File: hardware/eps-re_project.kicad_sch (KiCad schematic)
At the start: 50 parts, among them J1 2053380004, J13 53398-0671, J14 53398-0471, J2 2053380004, J21 205338-0002, J22 205338-0002, J25 205338-0002, J26 205338-0002, J27 205338-0002, J28 205338-0002, J29 205338-0002, J3 53398-0471, J4 2053380004, J5 53398-0471, J6 53398-0471, J7 53398-0471

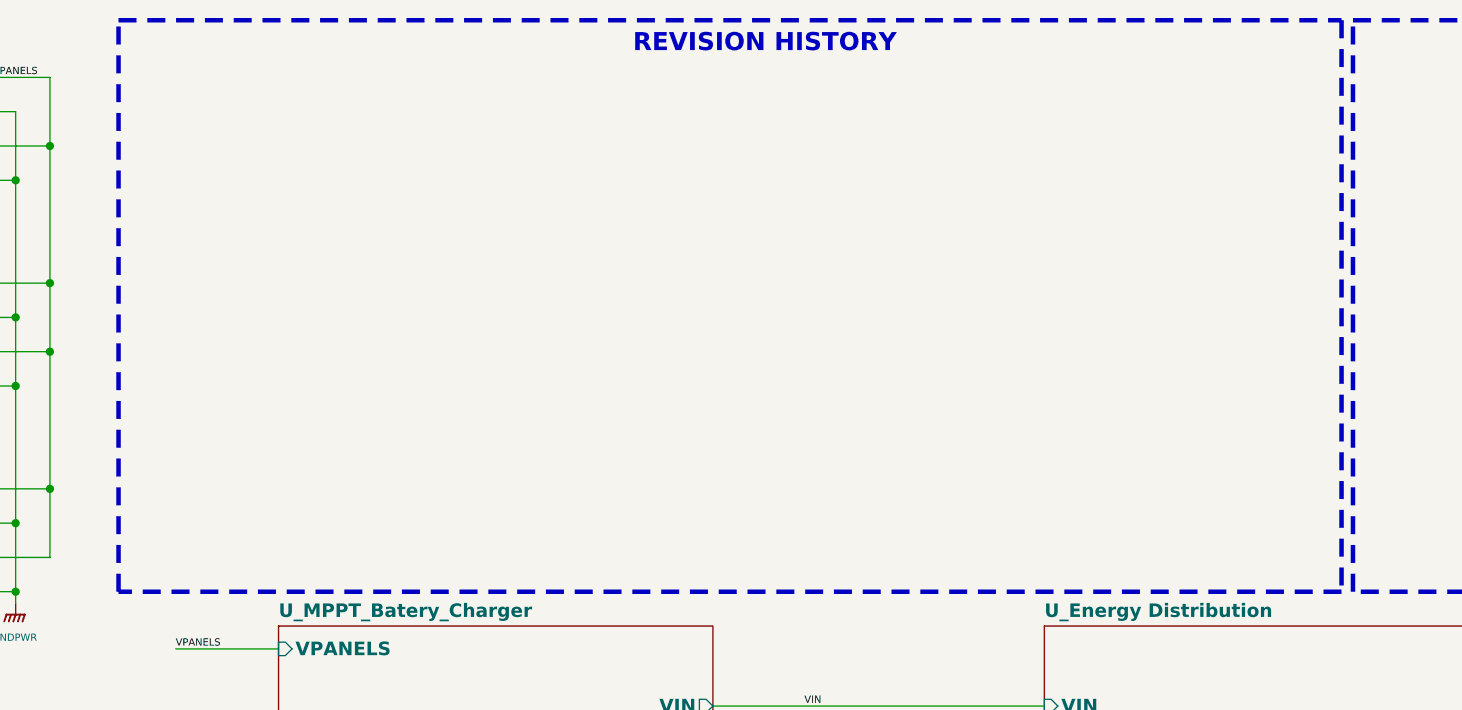
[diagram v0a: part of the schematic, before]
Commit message: hardware: Increasing the readability of the schematic and adding a table with the revision history
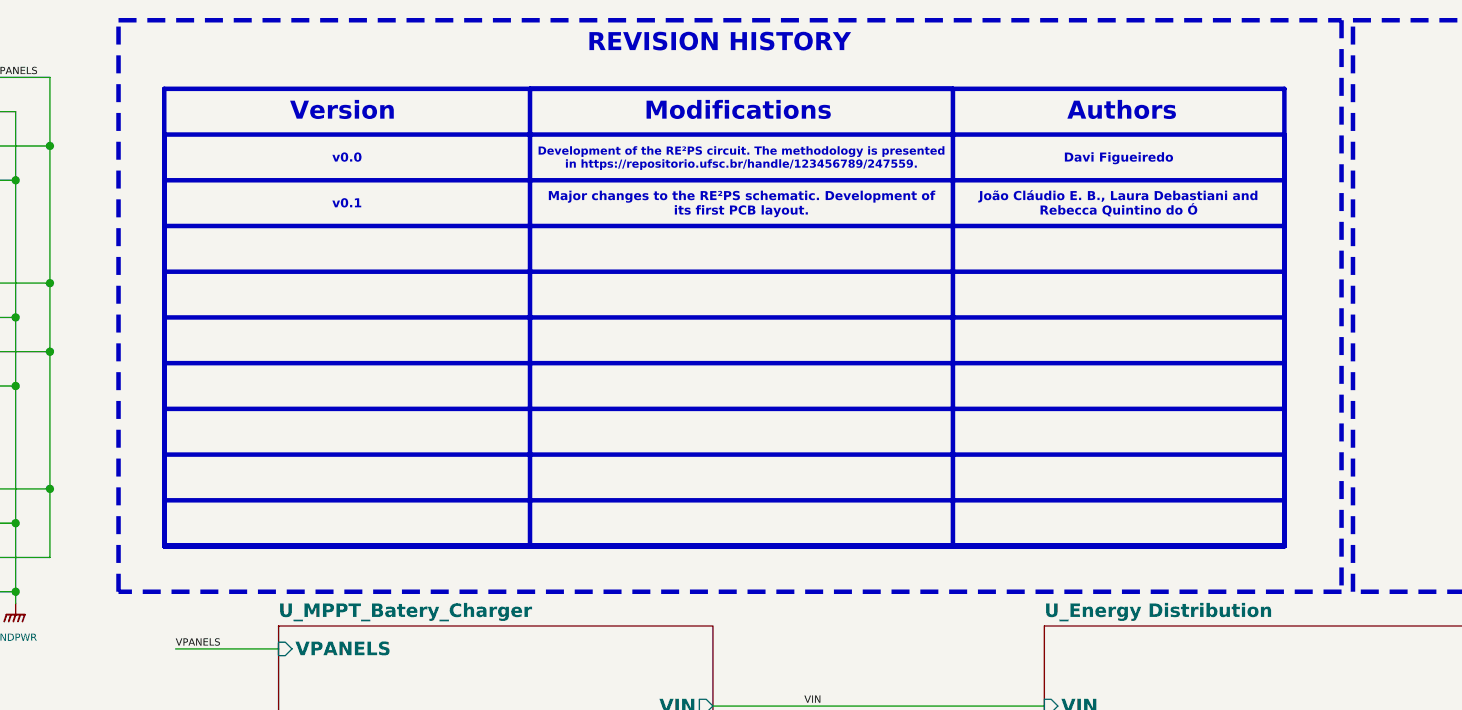
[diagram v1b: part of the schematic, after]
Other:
- note added: "Authors"
- note added: "Modifications"
- note added: "Version"
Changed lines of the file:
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@@
     (stroke (width 0) (type default))
+  )
+  (rectangle (start 66.04 58.42) (end 190.5 73.66)
+    (stroke (width 0.5) (type default) (color 0 0 0 1))
+    (fill (type none))
+  )
+  (rectangle (start 66.04 43.18) (end 190.5 73.66)
+    (stroke (width 0.5) (type default) (color 0 0 0 1))
+    (fill (type none))
   )
   (rectangle (start 198.12 15.24) (end 402.59 78.74)
     (stroke (width 0.5) (type dash) (color 0 0 0 1))
+    (fill (type none))
+  )
+  (rectangle (start 106.68 22.86) (end 153.67 73.66)
+    (stroke (width 0.5) (type default) (color 0 0 0 1))
+    (fill (type none))
+  )
+  (rectangle (start 66.04 68.58) (end 190.5 73.66)
+    (stroke (width 0.5) (type default) (color 0 0 0 1))
+    (fill (type none))
+  )
+  (rectangle (start 66.04 38.1) (end 190.5 73.66)
+    (stroke (width 0.5) (type default) (color 0 0 0 1))
     (fill (type none))
   )
@@
     (fill (type none))
   )
+  (rectangle (start 66.04 63.5) (end 190.5 73.66)
+    (stroke (width 0.5) (type default) (color 0 0 0 1))
+    (fill (type none))
+  )
+  (rectangle (start 66.04 22.86) (end 190.5 73.66)
+    (stroke (width 0.5) (type default) (color 0 0 0 1))
+    (fill (type none))
+  )
+  (rectangle (start 66.04 53.34) (end 190.5 73.66)
+    (stroke (width 0.5) (type default) (color 0 0 0 1))
+    (fill (type none))
+  )
+  (rectangle (start 66.04 33.02) (end 190.5 73.66)
+    (stroke (width 0.5) (type default) (color 0 0 0 1))
+    (fill (type none))
+  )
   (rectangle (start 12.7 254) (end 68.58 284.48)
     (stroke (width 0.5) (type dash) (color 0 0 0 1))
+    (fill (type none))
+  )
+  (rectangle (start 66.04 27.94) (end 190.5 73.66)
+    (stroke (width 0.5) (type default) (color 0 0 0 1))
+    (fill (type none))
+  )
+  (rectangle (start 66.04 48.26) (end 190.5 73.66)
+    (stroke (width 0.5) (type default) (color 0 0 0 1))
     (fill (type none))
   )
@@
     (stroke (width 0.5) (type dash) (color 0 0 0 1))
     (fill (type none))
+  )
+  (text_box "Davi Figueiredo"
+    (at 153.67 27.94 0) (size 36.83 5.08)
+    (stroke (width -0.0001) (type default))
+    (fill (type none))
+    (effects (font (size 1 1) (thickness 0.2) bold (color 0 0 0 1)))
+  )
+  (text_box "v0.0"
+    (at 66.04 27.94 0) (size 40.64 5.08)
+    (stroke (width -0.0001) (type default))
+    (fill (type none))
+    (effects (font (size 1 1) (thickness 0.2) bold (color 0 0 0 1)))
+  )
+  (text_box "Development of the RE²PS circuit. The methodology is presented in https://repositorio.ufsc.br/handle/123456789/247559."
+    (at 106.68 27.94 0) (size 46.99 5.08)
+    (stroke (width -0.0001) (type default))
+    (fill (type none))
+    (effects (font (size 0.9 0.9) (thickness 0.2) bold (color 0 0 0 1)))
+  )
+  (text_box "Major changes to the RE²PS schematic. Development of its first PCB layout."
+    (at 106.68 33.02 0) (size 46.99 5.08)
+    (stroke (width -0.0001) (type default))
+    (fill (type none))
+    (effects (font (size 1 1) (thickness 0.2) bold (color 0 0 0 1)))
+  )
+  (text_box "v0.1"
+    (at 66.04 33.02 0) (size 40.64 5.08)
+    (stroke (width -0.0001) (type default))
+    (fill (type none))
+    (effects (font (size 1 1) (thickness 0.2) bold (color 0 0 0 1)))
+  )
+  (text_box "João Cláudio E. B., Laura Debastiani and Rebecca Quintino do Ó"
+    (at 153.67 33.02 0) (size 36.83 5.08)
+    (stroke (width -0.0001) (type default))
+    (fill (type none))
+    (effects (font (size 1 1) (thickness 0.2) bold (color 0 0 0 1)))
+  )
+  (text "Version" (at 80.01 26.67 0)
+    (effects (font (size 2 2) (thickness 0.4) bold (color 0 0 0 1)) (justify left bottom))
+  )
+  (text "Authors" (at 166.37 26.67 0)
+    (effects (font (size 2 2) (thickness 0.4) bold (color 0 0 0 1)) (justify left bottom))
   )
   (text "BLOCK DIAGRAM" (at 297.18 19.05 0)
@@
     (effects (font (size 2 2) (thickness 0.4) bold (color 0 0 0 1)) (justify left bottom))
   )
-  (text "REVISION HISTORY" (at 118.11 19.05 0)
+  (text "REVISION HISTORY" (at 113.03 19.05 0)
     (effects (font (size 2 2) (thickness 0.4) bold (color 0 0 0 1)) (justify left bottom))
   )
+  (text "Modifications" (at 119.38 26.67 0)
+    (effects (font (size 2 2) (thickness 0.4) bold (color 0 0 0 1)) (justify left bottom))
+  )

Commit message: hardware: Making improvements for first release
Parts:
- D17, D18, D19, D20, D21, D22: MPN (none) -> CUHS20S40,H3F; Manufacturer (none) -> Toshiba; Manufacturer_Name Toshiba -> (none); Manufacturer_Part_Number CUHS20S40,H3F -> (none); Mouser Part Number 757-CUHS20S40H3F -> (none); Mouser Price/Stock https://www.mouser.co.uk/ProductDetail/Toshiba/CUHS20S40H3F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 -> (none); Package (none) -> US2H-2
- H1, H2, H3, H4: value MountingHole -> Mounting hole (3.2 mm); footprint MountingHole:MountingHole_3.2mm_M3_ISO14580_Pad -> footprints:MountingHole; symbol Mechanical:MountingHole -> MountingHole:MountingHole; MPN (none) -> N/A; Manufacturer (none) -> N/A; Package (none) -> N/A
- J1, J2, J4: MPN (none) -> 2053380004; Manufacturer (none) -> Molex; Package (none) -> Pico-Lock (4P); ambient temperature range high +105°C -> (none); ambient temperature range low -40°C -> (none); automotive No -> (none); category Conn -> (none); contact material Tin -> (none); current rating 1A -> (none); device class L1 Connectors -> (none); device class L2 Headers and Wire Housings -> (none); device class L3 unset -> (none); digikey description CONN HEADER SMD 4POS 1.25MM -> (none); digikey part number WM7608CT-ND -> (none); footprint url https://www.molex.com/pdm_docs/sd/533980471_sd.pdf -> (none); height 5.1mm -> (none); is connector yes -> (none); is male yes -> (none); lead free Yes -> (none); library id 4d2e3deedc0cf3e3 -> (none); manufacturer Molex -> (none); mouser part number 538-53398-0471 -> (none); number of contacts 4 -> (none); number of rows 1 -> (none); package HDR4 -> (none); pitch 1.25mm -> (none); rohs Yes -> (none); standoff height 0.05mm -> (none); temperature range high +105°C -> (none); temperature range low -40°C -> (none); voltage rating 125V -> (none)
- J13: value 53398-0671 -> 533980671; MPN (none) -> 533980671; Manufacturer (none) -> Molex; Package (none) -> PicoBlade (6P); category Conn -> (none); contact material Tin -> (none); current rating 1A -> (none); device class L1 Connectors -> (none); device class L2 Headers and Wire Housings -> (none); device class L3 unset -> (none); digikey description CONN HEADER 6POS 1.25MM VERT SMD -> (none); digikey part number WM7610CT-ND -> (none); height 4.9mm -> (none); is connector yes -> (none); is male yes -> (none); lead free yes -> (none); library id da45f97994f845ed -> (none); manufacturer Molex -> (none); mouser description Headers & Wire Housings VERTICAL HDR SMT 6P -> (none); mouser part number 538-53398-0671 -> (none); number of contacts 6 -> (none); number of rows 1 -> (none); package HDR6 -> (none); rohs yes -> (none); standoff height 0.05mm -> (none); temperature range high +85°C -> (none); temperature range low -40°C -> (none); voltage rating 125V -> (none)
- J14, J3, J5, J6, J7: value 53398-0471 -> 533980471; symbol 533980471:533980471_1 -> 533980471:533980471; MPN (none) -> 533980471; Manufacturer (none) -> Molex; Package (none) -> PicoBlade (4P); ambient temperature range high +105°C -> (none); ambient temperature range low -40°C -> (none); automotive No -> (none); category Conn -> (none); contact material Tin -> (none); current rating 1A -> (none); device class L1 Connectors -> (none); device class L2 Headers and Wire Housings -> (none); device class L3 unset -> (none); digikey description CONN HEADER SMD 4POS 1.25MM -> (none); digikey part number WM7608CT-ND -> (none); footprint url https://www.molex.com/pdm_docs/sd/533980471_sd.pdf -> (none); height 5.1mm -> (none); is connector yes -> (none); is male yes -> (none); lead free Yes -> (none); library id 4d2e3deedc0cf3e3 -> (none); manufacturer Molex -> (none); mouser part number 538-53398-0471 -> (none); number of contacts 4 -> (none); number of rows 1 -> (none); package HDR4 -> (none); pitch 1.25mm -> (none); rohs Yes -> (none); standoff height 0.05mm -> (none); temperature range high +105°C -> (none); temperature range low -40°C -> (none); voltage rating 125V -> (none)
- J21, J22, J25, J26, J27, J28, J29: value 205338-0002 -> 2053380002; MPN (none) -> 2053380002; Manufacturer (none) -> Molex; Package (none) -> Pico-Lock (2P); category Conn -> (none); contact material Tin -> (none); current rating 1A -> (none); device class L1 Connectors -> (none); device class L2 Headers and Wire Housings -> (none); device class L3 unset -> (none); digikey description CONN HEADER 2POS 1.25MM VERT SMD -> (none); digikey part number WM7606CT-ND -> (none); height 4.9mm -> (none); is connector yes -> (none); is male yes -> (none); lead free yes -> (none); library id bd646e8792f35d91 -> (none); manufacturer Molex -> (none); mouser description Conn Shrouded Header HDR 2 POS 1.25mm Solder ST SMD PicoBla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 -> (none); mouser part number 538-53398-0271 -> (none); number of contacts 2 -> (none); number of rows 1 -> (none); package HDR2 -> (none); rohs yes -> (none); standoff height 0.05mm -> (none); temperature range high +85°C -> (none); temperature range low -40°C -> (none); voltage rating 125V -> (none)
- TP1: value VPANELS -> Test point; MPN (none) -> N/A; Manufacturer (none) -> N/A; Package (none) -> N/A
- TP2: value BC_B_~{EN} -> Test point; MPN (none) -> N/A; Manufacturer (none) -> N/A; Package (none) -> N/A
- TP2: value BC_A_~{EN} -> Test point; MPN (none) -> N/A; Manufacturer (none) -> N/A; Package (none) -> N/A
- TP2: value 3V3_B_~{EN} -> Test point; MPN (none) -> N/A; Manufacturer (none) -> N/A; Package (none) -> N/A
- TP2: value 5V0_A_~{EN} -> Test point; MPN (none) -> N/A; Manufacturer (none) -> N/A; Package (none) -> N/A
- TP2: value 3V3_OBDH -> Test point; MPN (none) -> N/A; Manufacturer (none) -> N/A; Package (none) -> N/A
- TP2: value VBUS -> Test point; MPN (none) -> N/A; Manufacturer (none) -> N/A; Package (none) -> N/A
- TP2: value BC_VFB -> Test point; MPN (none) -> N/A; Manufacturer (none) -> N/A; Package (none) -> N/A
- TP2: value Payload_EN -> Test point; MPN (none) -> N/A; Manufacturer (none) -> N/A; Package (none) -> N/A
- TP2: value 5V0_Payload -> Test point; MPN (none) -> N/A; Manufacturer (none) -> N/A; Package (none) -> N/A
- TP2: value 5V0_RadioBeacon -> Test point; MPN (none) -> N/A; Manufacturer (none) -> N/A; Package (none) -> N/A
- TP2: value OBDH_EN -> Test point; MPN (none) -> N/A; Manufacturer (none) -> N/A; Package (none) -> N/A
- TP2: value RadioMain_EN -> Test point; MPN (none) -> N/A; Manufacturer (none) -> N/A; Package (none) -> N/A
- TP2: value BC_B_TS -> Test point; MPN (none) -> N/A; Manufacturer (none) -> N/A; Package (none) -> N/A
- TP2: value BC_A_TS -> Test point; MPN (none) -> N/A; Manufacturer (none) -> N/A; Package (none) -> N/A
- TP2: value 3V3_AntDep -> Test point; MPN (none) -> N/A; Manufacturer (none) -> N/A; Package (none) -> N/A
- TP2: value VIN -> Test point; MPN (none) -> N/A; Manufacturer (none) -> N/A; Package (none) -> N/A
- TP2: value 5V0_RadioMain -> Test point; MPN (none) -> N/A; Manufacturer (none) -> N/A; Package (none) -> N/A
- TP2: value Beacon_EN -> Test point; MPN (none) -> N/A; Manufacturer (none) -> N/A; Package (none) -> N/A
- TP2: value AntDep_EN -> Test point; MPN (none) -> N/A; Manufacturer (none) -> N/A; Package (none) -> N/A
- TP2: value 3V3_A_~{EN} -> Test point; MPN (none) -> N/A; Manufacturer (none) -> N/A; Package (none) -> N/A
- TP2: value 5V0_B_~{EN} -> Test point; MPN (none) -> N/A; Manufacturer (none) -> N/A; Package (none) -> N/A
- TP2: value RadioBeacon_EN -> Test point; MPN (none) -> N/A; Manufacturer (none) -> N/A; Package (none) -> N/A
- TP2: value 3V3_Beacon -> Test point; MPN (none) -> N/A; Manufacturer (none) -> N/A; Package (none) -> N/A
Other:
- moved on the sheet: H1, H2, H3, H4

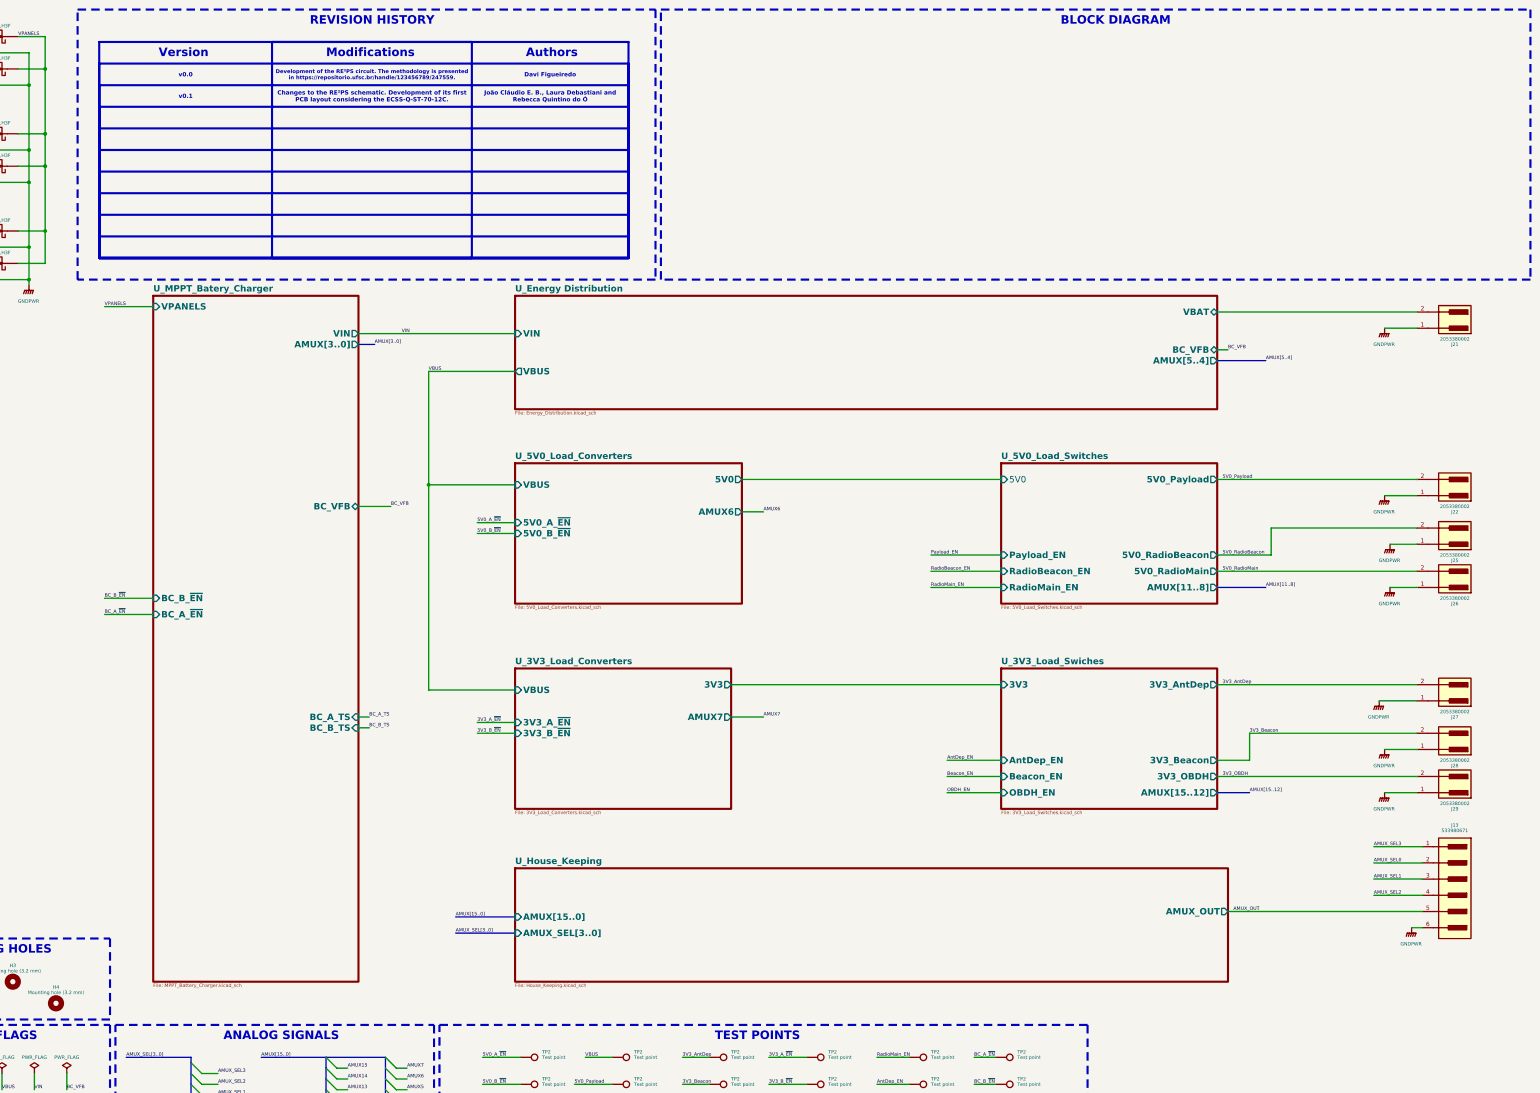
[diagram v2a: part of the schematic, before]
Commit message: hardware: Adding a block diagram of the RE²PS and making minor modifications to the symbols and schematic
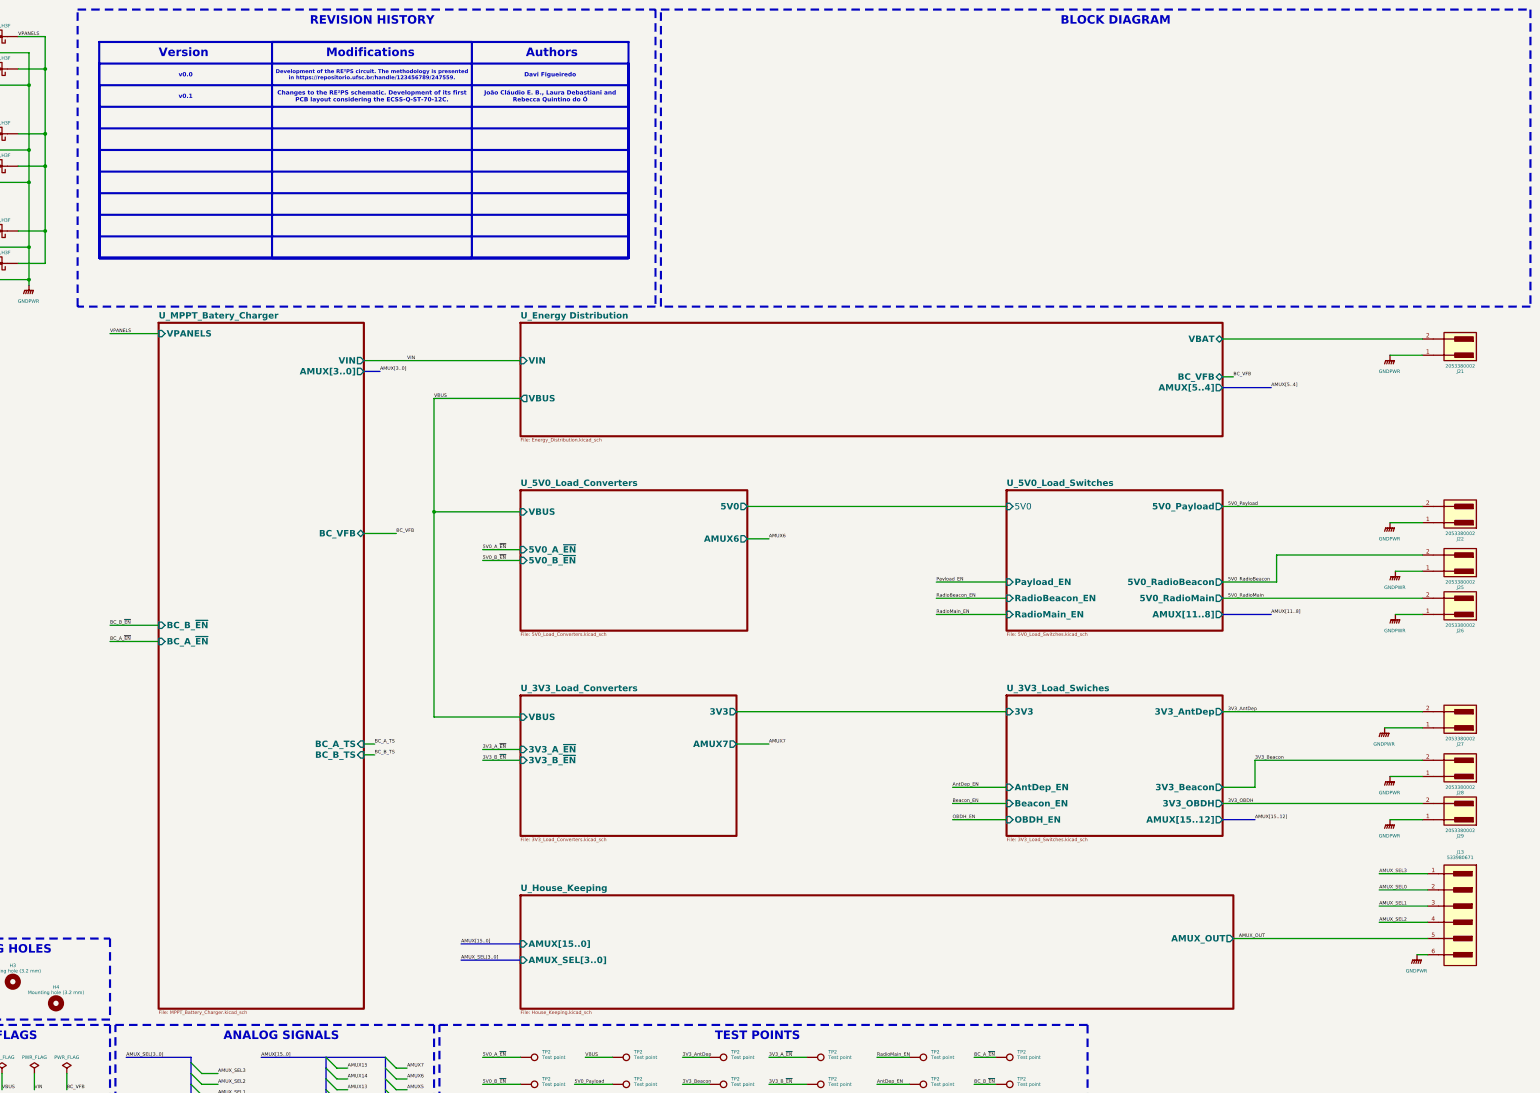
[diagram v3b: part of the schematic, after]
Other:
- moved on the sheet: J13, J21, J22, J25, J26, J27, J28, J29

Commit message: hardware: Minor modifications for the upcoming release
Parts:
- TP1, TP2: MPN N/A -> S2761-46R; Manufacturer N/A -> Harwin; Package N/A -> Non-standard
